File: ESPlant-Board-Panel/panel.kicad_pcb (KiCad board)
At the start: 2 copper layers, 84 x 143.7 mm, 207 parts, among them J1 Conn_01x05, U1 HC-TYPE-C-16P-01A-G, U13 ESP32-C6-MINI-1/U, U3 Reset, U4 Boot, U5 Temp/Humid-Sensor, U6 Light sensor, U7 AMS1117-3_3, U8 MK-12C02-G025

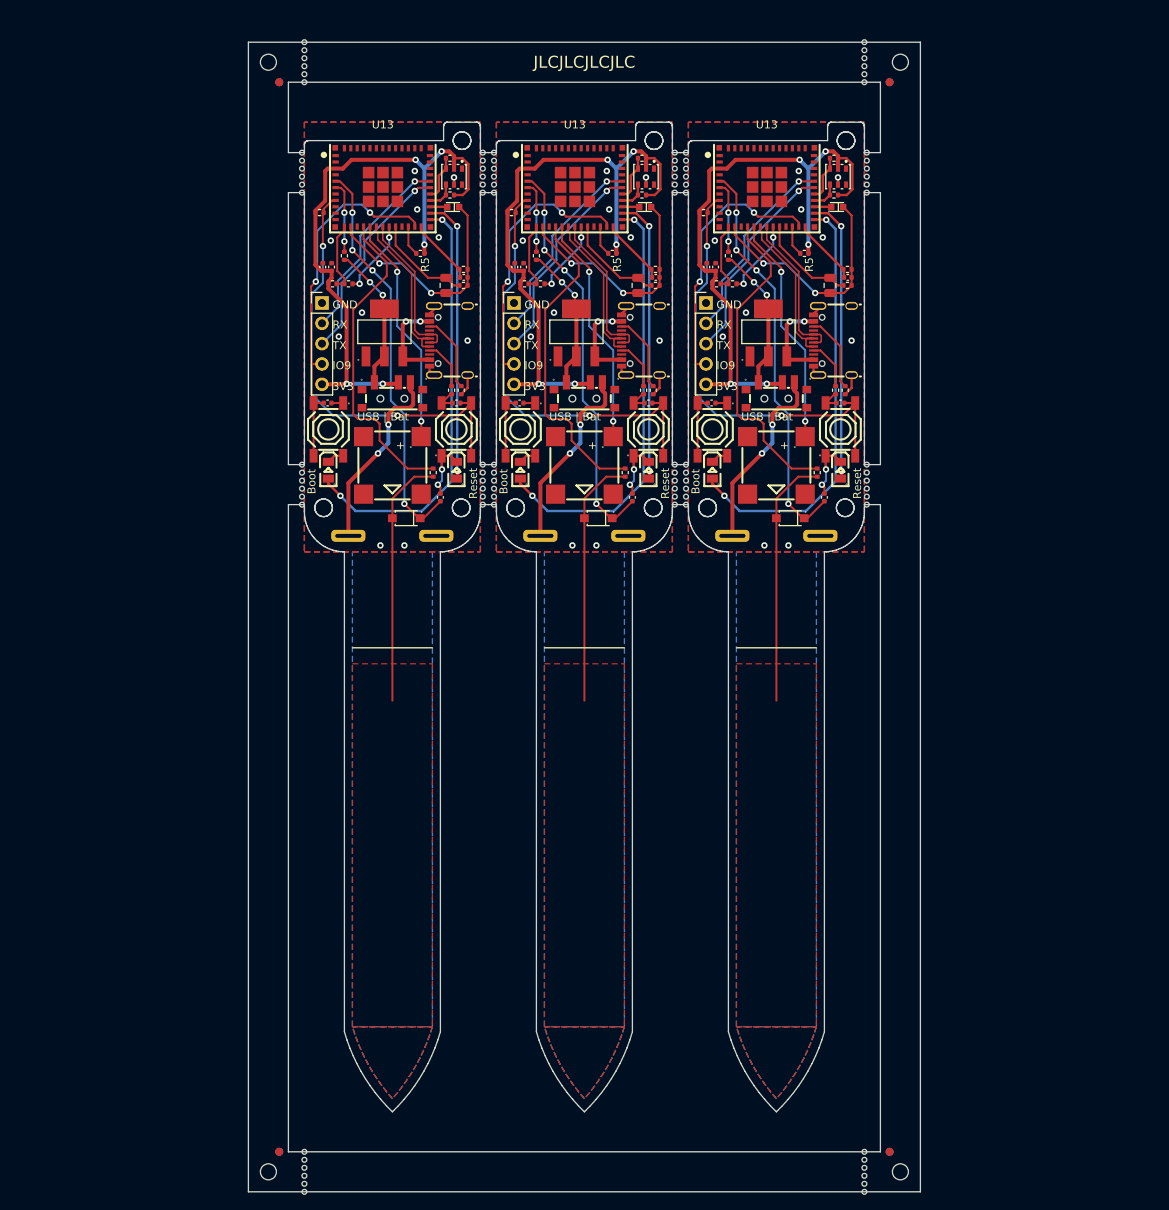
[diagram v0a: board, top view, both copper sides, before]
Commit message: Panel: Add panelization script
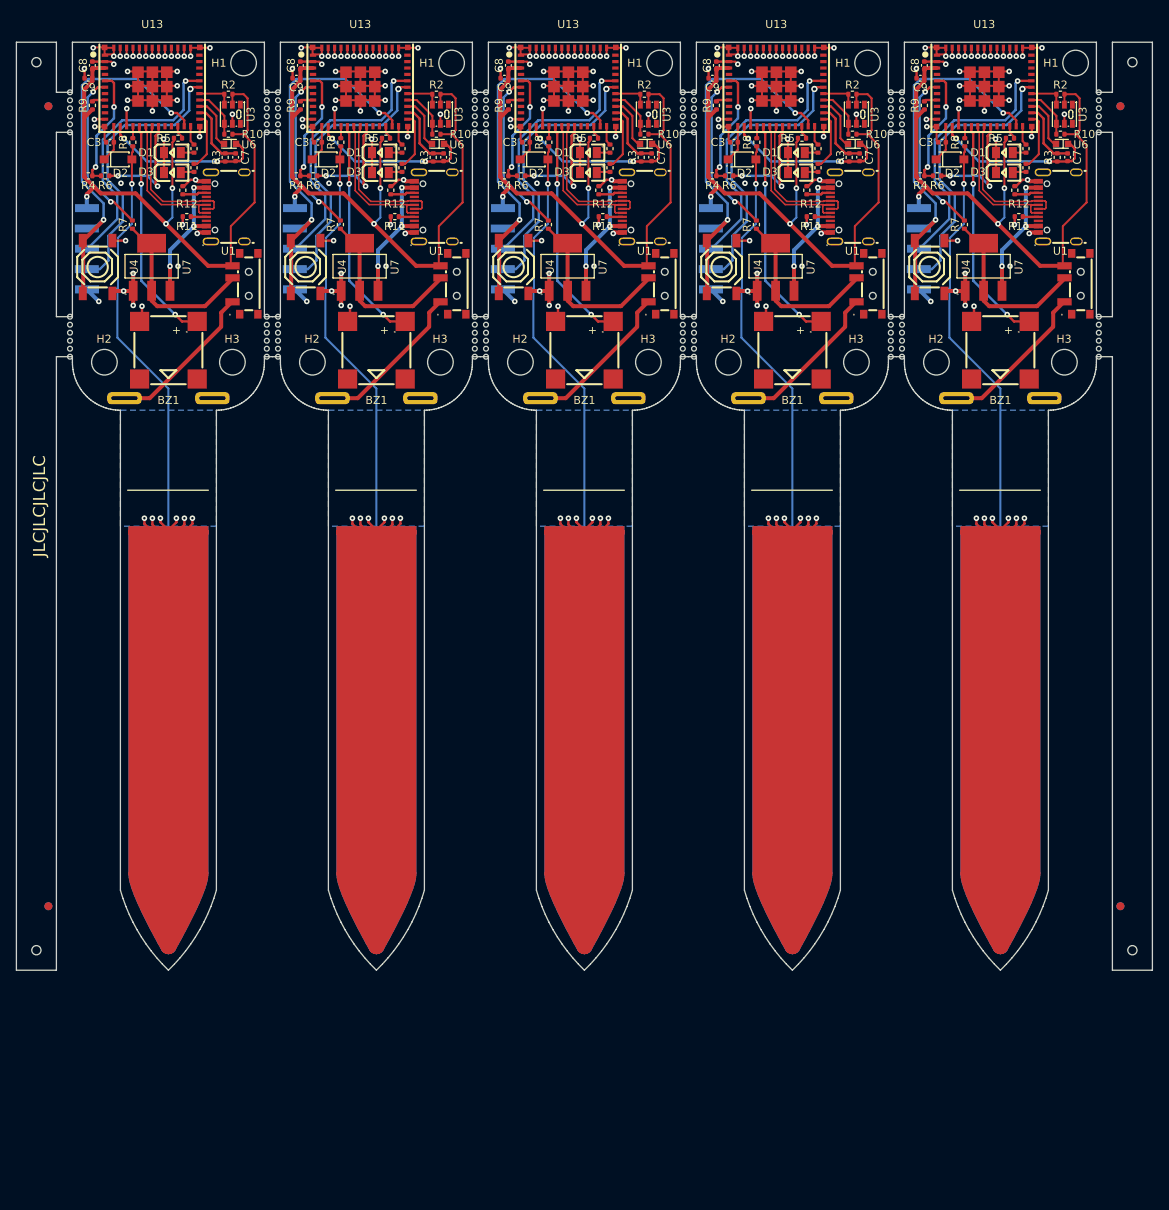
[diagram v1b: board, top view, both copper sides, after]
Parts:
- removed the BZ1 at (225.0, 72.9)
- removed the BZ1 at (201.0, 72.9)
- removed the BZ1 at (249.0, 72.9)
- removed C1 (x3), C2 (x3), C5 (x3): 100nF, Capacitor_SMD:C_0402_1005Metric
- removed the C3 at (207.0, 76.9)
- removed the C3 at (231.0, 76.9)
- removed the C3 at (255.0, 76.9)
- removed the C7 at (231.7, 50.4)
- removed the C7 at (255.7, 50.4)
- removed the C7 at (207.7, 50.4)
- removed the C8 at (193.4, 48.1)
- removed the C8 at (241.4, 48.1)
- removed the C8 at (217.4, 48.1)
- removed the C9 at (192.3, 48.1)
- removed the C9 at (240.3, 48.1)
- removed the C9 at (216.3, 48.1)
- removed the D1 at (217.0, 73.5)
- removed the D1 at (193.0, 73.5)
- removed the D1 at (241.0, 73.5)
- removed the D2 at (226.7, 79.5)
- removed the D2 at (202.7, 79.5)
- removed the D2 at (250.7, 79.5)
- removed the D3 at (209.0, 73.5)
- removed the D3 at (233.0, 73.5)
- removed the D3 at (257.0, 73.5)
- removed the J1 at (240.2, 52.6)
- removed the J1 at (216.2, 52.6)
- removed the J1 at (192.2, 52.6)
- removed R1 (x3): 10M, Resistor_SMD:R_0402_1005Metric
- removed the R10 at (256.2, 39.1)
- removed the R10 at (208.2, 39.1)
- removed the R10 at (232.2, 39.1)
- removed the R11 at (208.4, 63.5)
- removed the R11 at (232.4, 63.5)
- removed the R11 at (256.4, 63.5)
- removed the R12 at (233.6, 63.5)
- removed the R12 at (257.6, 63.5)
- removed the R12 at (209.6, 63.5)
- removed the R2 at (256.2, 34.5)
- removed the R2 at (208.2, 34.5)
- removed the R2 at (232.2, 34.5)
- removed the R3 at (233.9, 50.4)
- removed the R3 at (209.9, 50.4)
- removed the R3 at (257.9, 50.4)
- removed the R4 at (241.5, 50.2)
- removed the R4 at (217.5, 50.2)
- removed the R4 at (193.5, 50.2)
- removed the R5 at (228.5, 46.4)
- removed the R5 at (252.5, 46.4)
- removed the R5 at (204.5, 46.4)
- removed the R6 at (195.5, 50.2)
- removed the R6 at (243.5, 50.2)
- removed the R6 at (219.5, 50.2)
- removed the R7 at (219.0, 46.7)
- removed the R7 at (195.0, 46.7)
- removed the R7 at (243.0, 46.7)
- removed the R8 at (230.1, 73.8)
- removed the R8 at (254.1, 73.8)
- removed the R8 at (206.1, 73.8)
- removed the R9 at (191.9, 41.3)
- removed the R9 at (239.9, 41.3)
- removed the R9 at (215.9, 41.3)
- removed the U1 at (256.0, 57.3)
- removed the U1 at (232.0, 57.3)
- removed the U1 at (208.0, 57.3)
- removed the U13 at (247.8, 38.2)
- removed the U13 at (223.8, 38.2)
- removed the U13 at (199.8, 38.2)
- removed the U3 at (257.0, 68.4)
- removed the U3 at (209.0, 68.4)
- removed the U3 at (233.0, 68.4)
- removed the U4 at (193.0, 68.4)
- removed the U4 at (217.0, 68.4)
- removed the U4 at (241.0, 68.4)
- removed U5 (x3): Temp/Humid-Sensor, CustomFootprints:SENSOR-SMD_L3.0-W3.0-P1.00-BR
- removed the U6 at (232.6, 40.6)
- removed the U6 at (256.6, 40.6)
- removed the U6 at (208.6, 40.6)
- removed the U7 at (200.0, 56.3)
- removed the U7 at (224.0, 56.3)
- removed the U7 at (248.0, 56.3)
- removed the U8 at (201.0, 64.1)
- removed the U8 at (249.0, 64.1)
- removed the U8 at (225.0, 64.1)
- removed the U9 at (225.0, 81.7)
- removed the U9 at (249.0, 81.7)
- removed the U9 at (201.0, 81.7)
- added BZ1: Buzzer, CustomFootprints:BUZ-SMD_4P-L8.5-W8.5-P8.50-BR, F.Cu at (199.0, 58.5)
- added BZ1: Buzzer, CustomFootprints:BUZ-SMD_4P-L8.5-W8.5-P8.50-BR, F.Cu at (277.0, 58.5)
- added BZ1: Buzzer, CustomFootprints:BUZ-SMD_4P-L8.5-W8.5-P8.50-BR, F.Cu at (225.0, 58.5)
- added BZ1: Buzzer, CustomFootprints:BUZ-SMD_4P-L8.5-W8.5-P8.50-BR, F.Cu at (173.0, 58.5)
- added BZ1: Buzzer, CustomFootprints:BUZ-SMD_4P-L8.5-W8.5-P8.50-BR, F.Cu at (251.0, 58.5)
- added C3: 150pF, Capacitor_SMD:C_0402_1005Metric, F.Cu at (243.7, 32.5)
- added C3: 150pF, Capacitor_SMD:C_0402_1005Metric, F.Cu at (217.7, 32.5)
- added C3: 150pF, Capacitor_SMD:C_0402_1005Metric, F.Cu at (269.7, 32.5)
- added C3: 150pF, Capacitor_SMD:C_0402_1005Metric, F.Cu at (191.7, 32.5)
- added C3: 150pF, Capacitor_SMD:C_0402_1005Metric, F.Cu at (165.7, 32.5)
- added C4: 7pF-27pF, A=2.75cm^2, CustomFootprints:Sensor-Tip, B.Cu at (277.0, 81.0)
- added C4: 7pF-27pF, A=2.75cm^2, CustomFootprints:Sensor-Tip, B.Cu at (251.0, 81.0)
- added C4: 7pF-27pF, A=2.75cm^2, CustomFootprints:Sensor-Tip, B.Cu at (225.0, 81.0)
- added C4: 7pF-27pF, A=2.75cm^2, CustomFootprints:Sensor-Tip, B.Cu at (199.0, 81.0)
- added C4: 7pF-27pF, A=2.75cm^2, CustomFootprints:Sensor-Tip, B.Cu at (173.0, 81.0)
- added C7: 10uF, Capacitor_SMD:C_0402_1005Metric, F.Cu at (181.4, 34.4)
- added C7: 10uF, Capacitor_SMD:C_0402_1005Metric, F.Cu at (259.4, 34.4)
- added C7: 10uF, Capacitor_SMD:C_0402_1005Metric, F.Cu at (233.4, 34.4)
- added C7: 10uF, Capacitor_SMD:C_0402_1005Metric, F.Cu at (285.4, 34.4)
- added C7: 10uF, Capacitor_SMD:C_0402_1005Metric, F.Cu at (207.4, 34.4)
- added C8: 10nF, Capacitor_SMD:C_0402_1005Metric, F.Cu at (215.5, 22.9)
- added C8: 10nF, Capacitor_SMD:C_0402_1005Metric, F.Cu at (267.5, 22.9)
- added C8: 10nF, Capacitor_SMD:C_0402_1005Metric, F.Cu at (163.5, 22.9)
- added C8: 10nF, Capacitor_SMD:C_0402_1005Metric, F.Cu at (241.5, 22.9)
- added C8: 10nF, Capacitor_SMD:C_0402_1005Metric, F.Cu at (189.5, 22.9)
- added C9: 10uF, Capacitor_SMD:C_0402_1005Metric, F.Cu at (241.0, 24.5)
- added C9: 10uF, Capacitor_SMD:C_0402_1005Metric, F.Cu at (163.0, 24.5)
- added C9: 10uF, Capacitor_SMD:C_0402_1005Metric, F.Cu at (215.0, 24.5)
- added C9: 10uF, Capacitor_SMD:C_0402_1005Metric, F.Cu at (267.0, 24.5)
- added C9: 10uF, Capacitor_SMD:C_0402_1005Metric, F.Cu at (189.0, 24.5)
- added D1: GREEN, CustomFootprints:LED0805-R-RD, F.Cu at (199.5, 33.8)
- added D1: GREEN, CustomFootprints:LED0805-R-RD, F.Cu at (225.5, 33.8)
- added D1: GREEN, CustomFootprints:LED0805-R-RD, F.Cu at (251.5, 33.8)
- added D1: GREEN, CustomFootprints:LED0805-R-RD, F.Cu at (277.5, 33.8)
- added D1: GREEN, CustomFootprints:LED0805-R-RD, F.Cu at (173.5, 33.8)
- added D2: SOD-123-Switching-Diode, CustomFootprints:SOD-123F_L2.7-W1.6-LS3.8-RD, F.Cu at (166.7, 34.6)
- added D2: SOD-123-Switching-Diode, CustomFootprints:SOD-123F_L2.7-W1.6-LS3.8-RD, F.Cu at (270.7, 34.6)
- added D2: SOD-123-Switching-Diode, CustomFootprints:SOD-123F_L2.7-W1.6-LS3.8-RD, F.Cu at (218.7, 34.6)
- added D2: SOD-123-Switching-Diode, CustomFootprints:SOD-123F_L2.7-W1.6-LS3.8-RD, F.Cu at (192.7, 34.6)
- added D2: SOD-123-Switching-Diode, CustomFootprints:SOD-123F_L2.7-W1.6-LS3.8-RD, F.Cu at (244.7, 34.6)
- added D3: RED, CustomFootprints:LED0805-R-RD, F.Cu at (251.5, 36.3)
- added D3: RED, CustomFootprints:LED0805-R-RD, F.Cu at (173.5, 36.3)
- added D3: RED, CustomFootprints:LED0805-R-RD, F.Cu at (225.5, 36.3)
- added D3: RED, CustomFootprints:LED0805-R-RD, F.Cu at (199.5, 36.3)
- added D3: RED, CustomFootprints:LED0805-R-RD, F.Cu at (277.5, 36.3)
- added H1: MountingHole, MountingHole:MountingHole_3.2mm_M3, F.Cu at (182.4, 22.6)
- added H1: MountingHole, MountingHole:MountingHole_3.2mm_M3, F.Cu at (286.4, 22.6)
- added H1: MountingHole, MountingHole:MountingHole_3.2mm_M3, F.Cu at (234.4, 22.6)
- added H1: MountingHole, MountingHole:MountingHole_3.2mm_M3, F.Cu at (208.4, 22.6)
- added H1: MountingHole, MountingHole:MountingHole_3.2mm_M3, F.Cu at (260.4, 22.6)
- added H2: MountingHole, MountingHole:MountingHole_3.2mm_M3, F.Cu at (243.0, 60.0)
- added H2: MountingHole, MountingHole:MountingHole_3.2mm_M3, F.Cu at (217.0, 60.0)
- added H2: MountingHole, MountingHole:MountingHole_3.2mm_M3, F.Cu at (269.0, 60.0)
- added H2: MountingHole, MountingHole:MountingHole_3.2mm_M3, F.Cu at (191.0, 60.0)
- added H2: MountingHole, MountingHole:MountingHole_3.2mm_M3, F.Cu at (165.0, 60.0)
- added H3: MountingHole, MountingHole:MountingHole_3.2mm_M3, F.Cu at (181.0, 60.0)
- added H3: MountingHole, MountingHole:MountingHole_3.2mm_M3, F.Cu at (233.0, 60.0)
- added H3: MountingHole, MountingHole:MountingHole_3.2mm_M3, F.Cu at (285.0, 60.0)
- added H3: MountingHole, MountingHole:MountingHole_3.2mm_M3, F.Cu at (207.0, 60.0)
- added H3: MountingHole, MountingHole:MountingHole_3.2mm_M3, F.Cu at (259.0, 60.0)
- added J1: Conn_01x05, CustomFootprints:PinHeader_1x05_P2.54mm_Vertical_SMD, B.Cu at (216.1, 45.8)
- added J1: Conn_01x05, CustomFootprints:PinHeader_1x05_P2.54mm_Vertical_SMD, B.Cu at (164.1, 45.8)
- added J1: Conn_01x05, CustomFootprints:PinHeader_1x05_P2.54mm_Vertical_SMD, B.Cu at (268.1, 45.8)
- added J1: Conn_01x05, CustomFootprints:PinHeader_1x05_P2.54mm_Vertical_SMD, B.Cu at (242.1, 45.8)
- added J1: Conn_01x05, CustomFootprints:PinHeader_1x05_P2.54mm_Vertical_SMD, B.Cu at (190.1, 45.8)
- added KiKit_MB_17_1: NPTH, NPTH, F.Cu at (289.3, 31.3)
- added KiKit_MB_17_2: NPTH, NPTH, F.Cu at (289.3, 30.3)
- added KiKit_MB_17_3: NPTH, NPTH, F.Cu at (289.3, 29.3)
- added KiKit_MB_17_4: NPTH, NPTH, F.Cu at (289.3, 28.3)
- added KiKit_MB_17_5: NPTH, NPTH, F.Cu at (289.3, 27.3)
- added KiKit_MB_17_6: NPTH, NPTH, F.Cu at (289.3, 26.3)
- added KiKit_MB_18_1: NPTH, NPTH, F.Cu at (264.7, 26.3)
- added KiKit_MB_18_2: NPTH, NPTH, F.Cu at (264.7, 27.3)
- added KiKit_MB_18_3: NPTH, NPTH, F.Cu at (264.7, 28.3)
- added KiKit_MB_18_4: NPTH, NPTH, F.Cu at (264.7, 29.3)
- added KiKit_MB_18_5: NPTH, NPTH, F.Cu at (264.7, 30.3)
- added KiKit_MB_18_6: NPTH, NPTH, F.Cu at (264.7, 31.3)
- added KiKit_MB_19_1: NPTH, NPTH, F.Cu at (264.7, 54.3)
- added KiKit_MB_19_2: NPTH, NPTH, F.Cu at (264.7, 55.3)
- added KiKit_MB_19_3: NPTH, NPTH, F.Cu at (264.7, 56.3)
- added KiKit_MB_19_4: NPTH, NPTH, F.Cu at (264.7, 57.3)
- added KiKit_MB_19_5: NPTH, NPTH, F.Cu at (264.7, 58.3)
- added KiKit_MB_19_6: NPTH, NPTH, F.Cu at (264.7, 59.3)
- added KiKit_MB_20_1: NPTH, NPTH, F.Cu at (289.3, 59.3)
- added KiKit_MB_20_2: NPTH, NPTH, F.Cu at (289.3, 58.3)
- added KiKit_MB_20_3: NPTH, NPTH, F.Cu at (289.3, 57.3)
- added KiKit_MB_20_4: NPTH, NPTH, F.Cu at (289.3, 56.3)
- added KiKit_MB_20_5: NPTH, NPTH, F.Cu at (289.3, 55.3)
- added KiKit_MB_20_6: NPTH, NPTH, F.Cu at (289.3, 54.3)
- added R10: 5k1, Resistor_SMD:R_0402_1005Metric, F.Cu at (284.5, 31.5)
- added R10: 5k1, Resistor_SMD:R_0402_1005Metric, F.Cu at (258.5, 31.5)
- added R10: 5k1, Resistor_SMD:R_0402_1005Metric, F.Cu at (206.5, 31.5)
- added R10: 5k1, Resistor_SMD:R_0402_1005Metric, F.Cu at (232.5, 31.5)
- added R10: 5k1, Resistor_SMD:R_0402_1005Metric, F.Cu at (180.5, 31.5)
- added R11: 5k1, Resistor_SMD:R_0402_1005Metric, F.Cu at (279.3, 41.8)
- added R11: 5k1, Resistor_SMD:R_0402_1005Metric, F.Cu at (253.3, 41.8)
- added R11: 5k1, Resistor_SMD:R_0402_1005Metric, F.Cu at (175.3, 41.8)
- added R11: 5k1, Resistor_SMD:R_0402_1005Metric, F.Cu at (201.3, 41.8)
- added R11: 5k1, Resistor_SMD:R_0402_1005Metric, F.Cu at (227.3, 41.8)
- added R12: 5k1, Resistor_SMD:R_0402_1005Metric, F.Cu at (252.8, 38.5)
- added R12: 5k1, Resistor_SMD:R_0402_1005Metric, F.Cu at (174.8, 38.5)
- added R12: 5k1, Resistor_SMD:R_0402_1005Metric, F.Cu at (278.8, 38.5)
- added R12: 5k1, Resistor_SMD:R_0402_1005Metric, F.Cu at (226.8, 38.5)
- added R12: 5k1, Resistor_SMD:R_0402_1005Metric, F.Cu at (200.8, 38.5)
- added R13: 120, Resistor_SMD:R_0402_1005Metric, F.Cu at (176.2, 33.3)
- added R13: 120, Resistor_SMD:R_0402_1005Metric, F.Cu at (228.2, 33.3)
- added R13: 120, Resistor_SMD:R_0402_1005Metric, F.Cu at (202.2, 33.3)
- added R13: 120, Resistor_SMD:R_0402_1005Metric, F.Cu at (254.2, 33.3)
- added R13: 120, Resistor_SMD:R_0402_1005Metric, F.Cu at (280.2, 33.3)
- added R14: 120, Resistor_SMD:R_0402_1005Metric, F.Cu at (176.2, 35.7)
- added R14: 120, Resistor_SMD:R_0402_1005Metric, F.Cu at (254.2, 35.7)
- added R14: 120, Resistor_SMD:R_0402_1005Metric, F.Cu at (280.2, 35.7)
- added R14: 120, Resistor_SMD:R_0402_1005Metric, F.Cu at (228.2, 35.7)
- added R14: 120, Resistor_SMD:R_0402_1005Metric, F.Cu at (202.2, 35.7)
- added R2: 5k1, Resistor_SMD:R_0402_1005Metric, F.Cu at (232.5, 26.5)
- added R2: 5k1, Resistor_SMD:R_0402_1005Metric, F.Cu at (180.5, 26.5)
- added R2: 5k1, Resistor_SMD:R_0402_1005Metric, F.Cu at (258.5, 26.5)
- added R2: 5k1, Resistor_SMD:R_0402_1005Metric, F.Cu at (206.5, 26.5)
- added R2: 5k1, Resistor_SMD:R_0402_1005Metric, F.Cu at (284.5, 26.5)
- added R3: 47k, Resistor_SMD:R_0402_1005Metric, F.Cu at (232.1, 34.4)
- added R3: 47k, Resistor_SMD:R_0402_1005Metric, F.Cu at (206.1, 34.4)
- added R3: 47k, Resistor_SMD:R_0402_1005Metric, F.Cu at (284.1, 34.4)
- added R3: 47k, Resistor_SMD:R_0402_1005Metric, F.Cu at (180.1, 34.4)
- added R3: 47k, Resistor_SMD:R_0402_1005Metric, F.Cu at (258.1, 34.4)
- added R4: 5k1, Resistor_SMD:R_0402_1005Metric, F.Cu at (215.0, 36.7)
- added R4: 5k1, Resistor_SMD:R_0402_1005Metric, F.Cu at (241.0, 36.7)
- added R4: 5k1, Resistor_SMD:R_0402_1005Metric, F.Cu at (163.0, 36.7)
- added R4: 5k1, Resistor_SMD:R_0402_1005Metric, F.Cu at (267.0, 36.7)
- added R4: 5k1, Resistor_SMD:R_0402_1005Metric, F.Cu at (189.0, 36.7)
- added R5: 10k, Resistor_SMD:R_0402_1005Metric, F.Cu at (174.2, 32.0)
- added R5: 10k, Resistor_SMD:R_0402_1005Metric, F.Cu at (278.2, 32.0)
- added R5: 10k, Resistor_SMD:R_0402_1005Metric, F.Cu at (200.2, 32.0)
- added R5: 10k, Resistor_SMD:R_0402_1005Metric, F.Cu at (252.2, 32.0)
- added R5: 10k, Resistor_SMD:R_0402_1005Metric, F.Cu at (226.2, 32.0)
- added R6: 2k, Resistor_SMD:R_0402_1005Metric, F.Cu at (191.1, 36.7)
- added R6: 2k, Resistor_SMD:R_0402_1005Metric, F.Cu at (165.1, 36.7)
- added R6: 2k, Resistor_SMD:R_0402_1005Metric, F.Cu at (217.1, 36.7)
- added R6: 2k, Resistor_SMD:R_0402_1005Metric, F.Cu at (269.1, 36.7)
- added R6: 2k, Resistor_SMD:R_0402_1005Metric, F.Cu at (243.1, 36.7)
- added R7: 10k, Resistor_SMD:R_0402_1005Metric, F.Cu at (194.5, 42.8)
- added R7: 10k, Resistor_SMD:R_0402_1005Metric, F.Cu at (168.5, 42.8)
- added R7: 10k, Resistor_SMD:R_0402_1005Metric, F.Cu at (246.5, 42.8)
- added R7: 10k, Resistor_SMD:R_0402_1005Metric, F.Cu at (220.5, 42.8)
- added R7: 10k, Resistor_SMD:R_0402_1005Metric, F.Cu at (272.5, 42.8)
- added R8: 10k, Resistor_SMD:R_0402_1005Metric, F.Cu at (272.6, 32.5)
- added R8: 10k, Resistor_SMD:R_0402_1005Metric, F.Cu at (168.6, 32.5)
- added R8: 10k, Resistor_SMD:R_0402_1005Metric, F.Cu at (194.6, 32.5)
- added R8: 10k, Resistor_SMD:R_0402_1005Metric, F.Cu at (220.6, 32.5)
- added R8: 10k, Resistor_SMD:R_0402_1005Metric, F.Cu at (246.6, 32.5)
- added R9: 10k, Resistor_SMD:R_0402_1005Metric, F.Cu at (215.5, 27.9)
- added R9: 10k, Resistor_SMD:R_0402_1005Metric, F.Cu at (189.5, 27.9)
- added R9: 10k, Resistor_SMD:R_0402_1005Metric, F.Cu at (241.5, 27.9)
- added R9: 10k, Resistor_SMD:R_0402_1005Metric, F.Cu at (267.5, 27.9)
- added R9: 10k, Resistor_SMD:R_0402_1005Metric, F.Cu at (163.5, 27.9)
- added U1: HC-TYPE-C-16P-01A-G, CustomFootprints:USB-C-SMD_G-SWITCH_GT-USB-7010EN, F.Cu at (206.1, 40.6)
- added U1: HC-TYPE-C-16P-01A-G, CustomFootprints:USB-C-SMD_G-SWITCH_GT-USB-7010EN, F.Cu at (258.1, 40.6)
- added U1: HC-TYPE-C-16P-01A-G, CustomFootprints:USB-C-SMD_G-SWITCH_GT-USB-7010EN, F.Cu at (284.1, 40.6)
- added U1: HC-TYPE-C-16P-01A-G, CustomFootprints:USB-C-SMD_G-SWITCH_GT-USB-7010EN, F.Cu at (232.1, 40.6)
- added U1: HC-TYPE-C-16P-01A-G, CustomFootprints:USB-C-SMD_G-SWITCH_GT-USB-7010EN, F.Cu at (180.1, 40.6)
- added U13: ESP32-C6-MINI-1/U, CustomFootprints:WIFIM-SMD_61P-L16.6-W13.2-P0.80-ESP32-C6-MINI-1-N4, F.Cu at (275.0, 25.6)
- added U13: ESP32-C6-MINI-1/U, CustomFootprints:WIFIM-SMD_61P-L16.6-W13.2-P0.80-ESP32-C6-MINI-1-N4, F.Cu at (197.0, 25.6)
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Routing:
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- added copper zone on In1.Cu, net Board_0-GND
- added copper zone on In2.Cu, net Board_0-GND
- added copper zone on In1.Cu, net Board_1-GND
- added copper zone on In2.Cu, net Board_1-GND
- added copper zone on In1.Cu, net Board_2-GND
- added copper zone on In2.Cu, net Board_2-GND
- added copper zone on B.Cu, net Board_3-GND
- added copper zone on In1.Cu, net Board_3-GND
- added copper zone on In2.Cu, net Board_3-GND
- added copper zone on B.Cu, net Board_4-GND
- added copper zone on In1.Cu, net Board_4-GND
- added copper zone on In2.Cu, net Board_4-GND
- removed copper zone on F.Cu, net Board_0-/SensorCapV
- removed copper zone on F.Cu, net Board_0-GND
- removed copper zone on F.Cu, net Board_1-/SensorCapV
- removed copper zone on F.Cu, net Board_1-GND
- removed copper zone on F.Cu, net Board_2-/SensorCapV
- removed copper zone on F.Cu, net Board_2-GND
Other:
- board size 84 x 143.7 mm -> 142 x 116 mm
- copper layers 2 -> 4
- board text added: "Aconitum"
- board text added: "Blumy"
- board text removed: "3V3"
- board text removed: "Boot"
- board text removed: "ESPlant-v2.1"
- board text removed: "GND"
- board text removed: "IO9"
- board text removed: "M2"
- board text removed: "RX"
- board text removed: "Reset"
- board text removed: "TX"
- board text removed: "USB | Bat"

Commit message: Board: New power supply chip
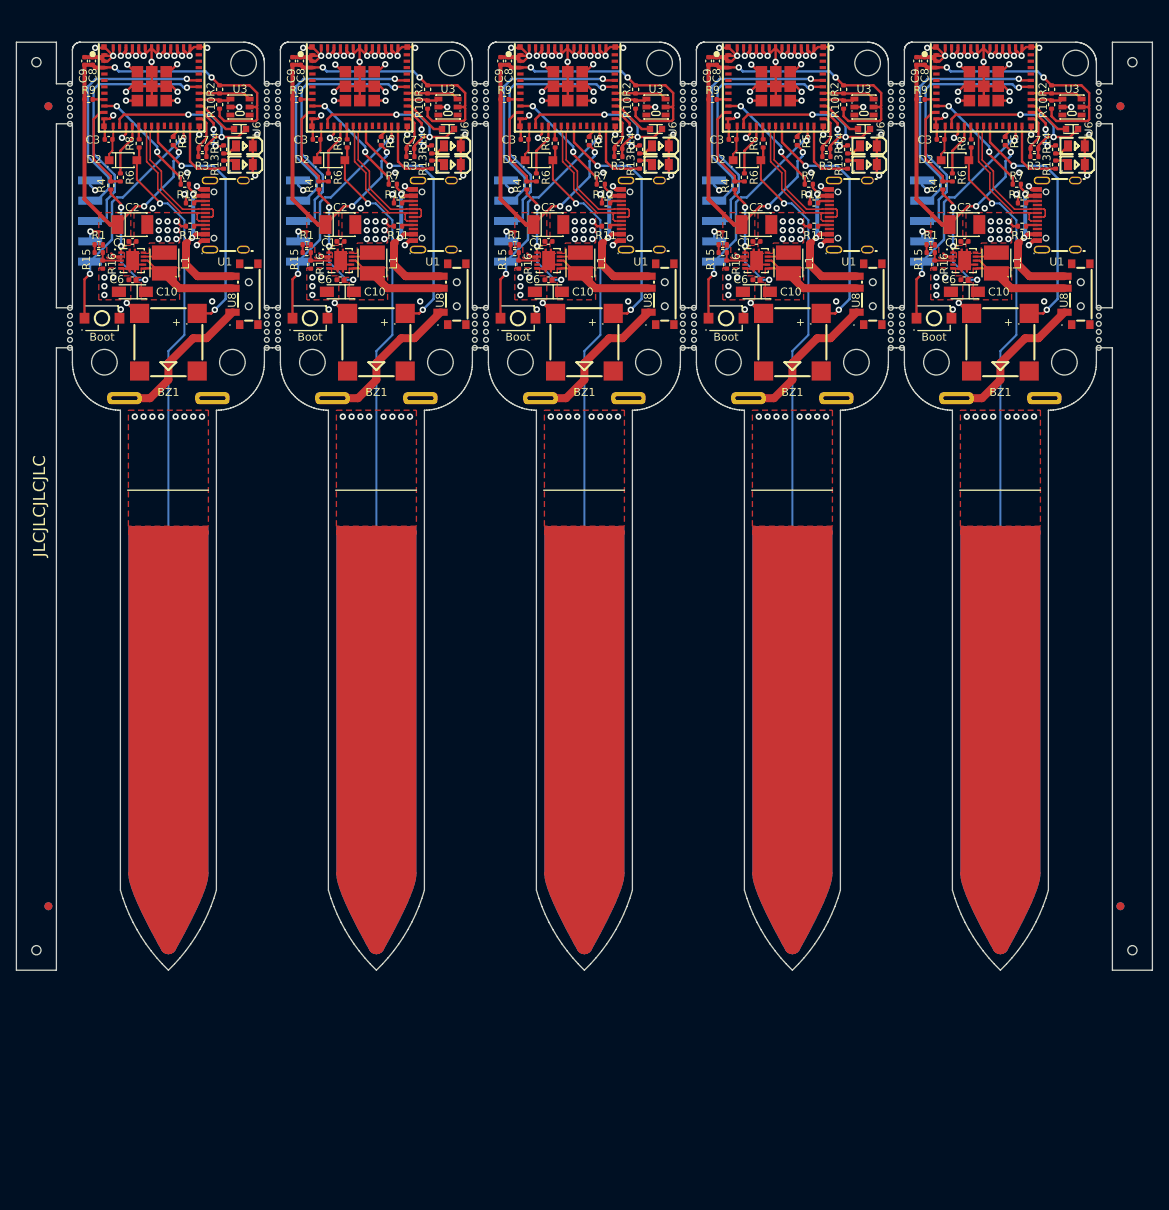
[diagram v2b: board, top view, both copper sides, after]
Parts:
- removed the BZ1 at (199.0, 58.5)
- removed the BZ1 at (277.0, 58.5)
- removed the BZ1 at (225.0, 58.5)
- removed the BZ1 at (173.0, 58.5)
- removed the BZ1 at (251.0, 58.5)
- removed the C3 at (243.7, 32.5)
- removed the C3 at (217.7, 32.5)
- removed the C3 at (269.7, 32.5)
- removed the C3 at (191.7, 32.5)
- removed the C3 at (165.7, 32.5)
- removed the C7 at (181.4, 34.4)
- removed the C7 at (259.4, 34.4)
- removed the C7 at (233.4, 34.4)
- removed the C7 at (285.4, 34.4)
- removed the C7 at (207.4, 34.4)
- removed the C8 at (215.5, 22.9)
- removed the C8 at (267.5, 22.9)
- removed the C8 at (163.5, 22.9)
- removed the C8 at (241.5, 22.9)
- removed the C8 at (189.5, 22.9)
- removed the C9 at (241.0, 24.5)
- removed the C9 at (163.0, 24.5)
- removed the C9 at (215.0, 24.5)
- removed the C9 at (267.0, 24.5)
- removed the C9 at (189.0, 24.5)
- removed the D1 at (199.5, 33.8)
- removed the D1 at (225.5, 33.8)
- removed the D1 at (251.5, 33.8)
- removed the D1 at (277.5, 33.8)
- removed the D1 at (173.5, 33.8)
- removed the D2 at (166.7, 34.6)
- removed the D2 at (270.7, 34.6)
- removed the D2 at (218.7, 34.6)
- removed the D2 at (192.7, 34.6)
- removed the D2 at (244.7, 34.6)
- removed the D3 at (251.5, 36.3)
- removed the D3 at (173.5, 36.3)
- removed the D3 at (225.5, 36.3)
- removed the D3 at (199.5, 36.3)
- removed the D3 at (277.5, 36.3)
- removed the J1 at (216.1, 45.8)
- removed the J1 at (164.1, 45.8)
- removed the J1 at (268.1, 45.8)
- removed the J1 at (242.1, 45.8)
- removed the J1 at (190.1, 45.8)
- removed the R10 at (284.5, 31.5)
- removed the R10 at (258.5, 31.5)
- removed the R10 at (206.5, 31.5)
- removed the R10 at (232.5, 31.5)
- removed the R10 at (180.5, 31.5)
- removed the R11 at (279.3, 41.8)
- removed the R11 at (253.3, 41.8)
- removed the R11 at (175.3, 41.8)
- removed the R11 at (201.3, 41.8)
- removed the R11 at (227.3, 41.8)
- removed the R12 at (252.8, 38.5)
- removed the R12 at (174.8, 38.5)
- removed the R12 at (278.8, 38.5)
- removed the R12 at (226.8, 38.5)
- removed the R12 at (200.8, 38.5)
- removed the R13 at (176.2, 33.3)
- removed the R13 at (228.2, 33.3)
- removed the R13 at (202.2, 33.3)
- removed the R13 at (254.2, 33.3)
- removed the R13 at (280.2, 33.3)
- removed the R14 at (176.2, 35.7)
- removed the R14 at (254.2, 35.7)
- removed the R14 at (280.2, 35.7)
- removed the R14 at (228.2, 35.7)
- removed the R14 at (202.2, 35.7)
- removed the R2 at (232.5, 26.5)
- removed the R2 at (180.5, 26.5)
- removed the R2 at (258.5, 26.5)
- removed the R2 at (206.5, 26.5)
- removed the R2 at (284.5, 26.5)
- removed the R3 at (232.1, 34.4)
- removed the R3 at (206.1, 34.4)
- removed the R3 at (284.1, 34.4)
- removed the R3 at (180.1, 34.4)
- removed the R3 at (258.1, 34.4)
- removed the R4 at (215.0, 36.7)
- removed the R4 at (241.0, 36.7)
- removed the R4 at (163.0, 36.7)
- removed the R4 at (267.0, 36.7)
- removed the R4 at (189.0, 36.7)
- removed the R5 at (174.2, 32.0)
- removed the R5 at (278.2, 32.0)
- removed the R5 at (200.2, 32.0)
- removed the R5 at (252.2, 32.0)
- removed the R5 at (226.2, 32.0)
- removed the R6 at (191.1, 36.7)
- removed the R6 at (165.1, 36.7)
- removed the R6 at (217.1, 36.7)
- removed the R6 at (269.1, 36.7)
- removed the R6 at (243.1, 36.7)
- removed the R7 at (194.5, 42.8)
- removed the R7 at (168.5, 42.8)
- removed the R7 at (246.5, 42.8)
- removed the R7 at (220.5, 42.8)
- removed the R7 at (272.5, 42.8)
- removed the R8 at (272.6, 32.5)
- removed the R8 at (168.6, 32.5)
- removed the R8 at (194.6, 32.5)
- removed the R8 at (220.6, 32.5)
- removed the R8 at (246.6, 32.5)
- removed the R9 at (215.5, 27.9)
- removed the R9 at (189.5, 27.9)
- removed the R9 at (241.5, 27.9)
- removed the R9 at (267.5, 27.9)
- removed the R9 at (163.5, 27.9)
- removed the U1 at (206.1, 40.6)
- removed the U1 at (258.1, 40.6)
- removed the U1 at (284.1, 40.6)
- removed the U1 at (232.1, 40.6)
- removed the U1 at (180.1, 40.6)
- removed the U13 at (275.0, 25.6)
- removed the U13 at (197.0, 25.6)
- removed the U13 at (223.0, 25.6)
- removed the U13 at (171.0, 25.6)
- removed the U13 at (249.0, 25.6)
- removed the U3 at (285.0, 29.0)
- removed the U3 at (233.0, 29.0)
- removed the U3 at (207.0, 29.0)
- removed the U3 at (181.0, 29.0)
- removed the U3 at (259.0, 29.0)
- removed U4 (x5): Button, CustomFootprints:SW-SMD_4P-L5.1-W5.1-P3.70-LS6.5-TL-2
- removed the U6 at (284.7, 32.7)
- removed the U6 at (206.7, 32.7)
- removed the U6 at (258.7, 32.7)
- removed the U6 at (180.7, 32.7)
- removed the U6 at (232.7, 32.7)
- removed the U7 at (170.9, 48.1)
- removed the U7 at (274.9, 48.1)
- removed the U7 at (222.9, 48.1)
- removed the U7 at (196.9, 48.1)
- removed the U7 at (248.9, 48.1)
- removed the U8 at (208.6, 50.2)
- removed the U8 at (286.6, 50.2)
- removed the U8 at (260.6, 50.2)
- removed the U8 at (234.6, 50.2)
- removed the U8 at (182.6, 50.2)
- added BZ1: Buzzer, CustomFootprints:BUZ-SMD_4P-L8.5-W8.5-P8.50-BR, F.Cu at (277.0, 57.5)
- added BZ1: Buzzer, CustomFootprints:BUZ-SMD_4P-L8.5-W8.5-P8.50-BR, F.Cu at (251.0, 57.5)
- added BZ1: Buzzer, CustomFootprints:BUZ-SMD_4P-L8.5-W8.5-P8.50-BR, F.Cu at (225.0, 57.5)
- added BZ1: Buzzer, CustomFootprints:BUZ-SMD_4P-L8.5-W8.5-P8.50-BR, F.Cu at (199.0, 57.5)
- added BZ1: Buzzer, CustomFootprints:BUZ-SMD_4P-L8.5-W8.5-P8.50-BR, F.Cu at (173.0, 57.5)
- added C1: 2.2uF-Ceramic, Capacitor_SMD:C_0402_1005Metric, F.Cu at (168.5, 44.9)
- added C1: 2.2uF-Ceramic, Capacitor_SMD:C_0402_1005Metric, F.Cu at (220.5, 44.9)
- added C1: 2.2uF-Ceramic, Capacitor_SMD:C_0402_1005Metric, F.Cu at (272.5, 44.9)
- added C1: 2.2uF-Ceramic, Capacitor_SMD:C_0402_1005Metric, F.Cu at (194.5, 44.9)
- added C1: 2.2uF-Ceramic, Capacitor_SMD:C_0402_1005Metric, F.Cu at (246.5, 44.9)
- added C10: 10uF-Tantalum, CustomFootprints:CAP-SMD_L3.2-W1.6-RD-C7171, F.Cu at (220.5, 51.2)
- added C10: 10uF-Tantalum, CustomFootprints:CAP-SMD_L3.2-W1.6-RD-C7171, F.Cu at (272.5, 51.2)
- added C10: 10uF-Tantalum, CustomFootprints:CAP-SMD_L3.2-W1.6-RD-C7171, F.Cu at (194.5, 51.2)
- added C10: 10uF-Tantalum, CustomFootprints:CAP-SMD_L3.2-W1.6-RD-C7171, F.Cu at (246.5, 51.2)
- added C10: 10uF-Tantalum, CustomFootprints:CAP-SMD_L3.2-W1.6-RD-C7171, F.Cu at (168.5, 51.2)
- added C2: 100uF-Tantalum, CustomFootprints:CASE-B_3528, F.Cu at (168.5, 42.8)
- added C2: 100uF-Tantalum, CustomFootprints:CASE-B_3528, F.Cu at (194.5, 42.8)
- added C2: 100uF-Tantalum, CustomFootprints:CASE-B_3528, F.Cu at (272.5, 42.8)
- added C2: 100uF-Tantalum, CustomFootprints:CASE-B_3528, F.Cu at (246.5, 42.8)
- added C2: 100uF-Tantalum, CustomFootprints:CASE-B_3528, F.Cu at (220.5, 42.8)
- added C3: 10nF, Capacitor_SMD:C_0402_1005Metric, F.Cu at (217.5, 32.2)
- added C3: 10nF, Capacitor_SMD:C_0402_1005Metric, F.Cu at (165.5, 32.2)
- added C3: 10nF, Capacitor_SMD:C_0402_1005Metric, F.Cu at (243.5, 32.2)
- added C3: 10nF, Capacitor_SMD:C_0402_1005Metric, F.Cu at (191.5, 32.2)
- added C3: 10nF, Capacitor_SMD:C_0402_1005Metric, F.Cu at (269.5, 32.2)
- added C6: 100nF-Ceramic, Capacitor_SMD:C_0402_1005Metric, F.Cu at (220.5, 49.7)
- added C6: 100nF-Ceramic, Capacitor_SMD:C_0402_1005Metric, F.Cu at (246.5, 49.7)
- added C6: 100nF-Ceramic, Capacitor_SMD:C_0402_1005Metric, F.Cu at (168.5, 49.7)
- added C6: 100nF-Ceramic, Capacitor_SMD:C_0402_1005Metric, F.Cu at (194.5, 49.7)
- added C6: 100nF-Ceramic, Capacitor_SMD:C_0402_1005Metric, F.Cu at (272.5, 49.7)
- added C7: 10uF, Capacitor_SMD:C_0402_1005Metric, F.Cu at (229.3, 33.3)
- added C7: 10uF, Capacitor_SMD:C_0402_1005Metric, F.Cu at (203.3, 33.3)
- added C7: 10uF, Capacitor_SMD:C_0402_1005Metric, F.Cu at (281.3, 33.3)
- added C7: 10uF, Capacitor_SMD:C_0402_1005Metric, F.Cu at (177.3, 33.3)
- added C7: 10uF, Capacitor_SMD:C_0402_1005Metric, F.Cu at (255.3, 33.3)
- added C8: 10nF, Capacitor_SMD:C_0402_1005Metric, F.Cu at (267.5, 22.4)
- added C8: 10nF, Capacitor_SMD:C_0402_1005Metric, F.Cu at (215.5, 22.4)
- added C8: 10nF, Capacitor_SMD:C_0402_1005Metric, F.Cu at (241.5, 22.4)
- added C8: 10nF, Capacitor_SMD:C_0402_1005Metric, F.Cu at (163.5, 22.4)
- added C8: 10nF, Capacitor_SMD:C_0402_1005Metric, F.Cu at (189.5, 22.4)
- added C9: 10uF, Capacitor_SMD:C_0402_1005Metric, F.Cu at (162.5, 22.4)
- added C9: 10uF, Capacitor_SMD:C_0402_1005Metric, F.Cu at (214.5, 22.4)
- added C9: 10uF, Capacitor_SMD:C_0402_1005Metric, F.Cu at (266.5, 22.4)
- added C9: 10uF, Capacitor_SMD:C_0402_1005Metric, F.Cu at (188.5, 22.4)
- added C9: 10uF, Capacitor_SMD:C_0402_1005Metric, F.Cu at (240.5, 22.4)
- added D1: GREEN, CustomFootprints:LED0805-R-RD, F.Cu at (234.5, 35.3)
- added D1: GREEN, CustomFootprints:LED0805-R-RD, F.Cu at (182.5, 35.3)
- added D1: GREEN, CustomFootprints:LED0805-R-RD, F.Cu at (208.5, 35.3)
- added D1: GREEN, CustomFootprints:LED0805-R-RD, F.Cu at (286.5, 35.3)
- added D1: GREEN, CustomFootprints:LED0805-R-RD, F.Cu at (260.5, 35.3)
- added D2: SOD-123-Switching-Diode, CustomFootprints:SOD-123F_L2.7-W1.6-LS3.8-RD, F.Cu at (193.3, 34.8)
- added D2: SOD-123-Switching-Diode, CustomFootprints:SOD-123F_L2.7-W1.6-LS3.8-RD, F.Cu at (167.3, 34.8)
- added D2: SOD-123-Switching-Diode, CustomFootprints:SOD-123F_L2.7-W1.6-LS3.8-RD, F.Cu at (271.3, 34.8)
- added D2: SOD-123-Switching-Diode, CustomFootprints:SOD-123F_L2.7-W1.6-LS3.8-RD, F.Cu at (219.3, 34.8)
- added D2: SOD-123-Switching-Diode, CustomFootprints:SOD-123F_L2.7-W1.6-LS3.8-RD, F.Cu at (245.3, 34.8)
- added D3: RED, CustomFootprints:LED0805-R-RD, F.Cu at (208.5, 33.0)
- added D3: RED, CustomFootprints:LED0805-R-RD, F.Cu at (260.5, 33.0)
- added D3: RED, CustomFootprints:LED0805-R-RD, F.Cu at (182.5, 33.0)
- added D3: RED, CustomFootprints:LED0805-R-RD, F.Cu at (234.5, 33.0)
- added D3: RED, CustomFootprints:LED0805-R-RD, F.Cu at (286.5, 33.0)
- added J1: Conn_01x05, CustomFootprints:PinHeader_1x05_P2.54mm_Vertical_SMD, B.Cu at (265.9, 42.4)
- added J1: Conn_01x05, CustomFootprints:PinHeader_1x05_P2.54mm_Vertical_SMD, B.Cu at (213.9, 42.4)
- added J1: Conn_01x05, CustomFootprints:PinHeader_1x05_P2.54mm_Vertical_SMD, B.Cu at (161.9, 42.4)
- added J1: Conn_01x05, CustomFootprints:PinHeader_1x05_P2.54mm_Vertical_SMD, B.Cu at (239.9, 42.4)
- added J1: Conn_01x05, CustomFootprints:PinHeader_1x05_P2.54mm_Vertical_SMD, B.Cu at (187.9, 42.4)
- added L1: CD32YP0302-6R8M, CustomFootprints:IND-SMD_L3.5-W3.0, F.Cu at (172.5, 47.6)
- added L1: CD32YP0302-6R8M, CustomFootprints:IND-SMD_L3.5-W3.0, F.Cu at (224.5, 47.6)
- added L1: CD32YP0302-6R8M, CustomFootprints:IND-SMD_L3.5-W3.0, F.Cu at (276.5, 47.6)
- added L1: CD32YP0302-6R8M, CustomFootprints:IND-SMD_L3.5-W3.0, F.Cu at (250.5, 47.6)
- added L1: CD32YP0302-6R8M, CustomFootprints:IND-SMD_L3.5-W3.0, F.Cu at (198.5, 47.6)
- added R1: 100k, Resistor_SMD:R_0402_1005Metric, F.Cu at (268.3, 45.3)
- added R1: 100k, Resistor_SMD:R_0402_1005Metric, F.Cu at (190.3, 45.3)
- added R1: 100k, Resistor_SMD:R_0402_1005Metric, F.Cu at (216.3, 45.3)
- added R1: 100k, Resistor_SMD:R_0402_1005Metric, F.Cu at (242.3, 45.3)
- added R1: 100k, Resistor_SMD:R_0402_1005Metric, F.Cu at (164.3, 45.3)
- added R10: 5k1, Resistor_SMD:R_0402_1005Metric, F.Cu at (205.4, 27.8)
- added R10: 5k1, Resistor_SMD:R_0402_1005Metric, F.Cu at (179.4, 27.8)
- added R10: 5k1, Resistor_SMD:R_0402_1005Metric, F.Cu at (257.4, 27.8)
- added R10: 5k1, Resistor_SMD:R_0402_1005Metric, F.Cu at (283.4, 27.8)
- added R10: 5k1, Resistor_SMD:R_0402_1005Metric, F.Cu at (231.4, 27.8)
- added R11: 5k1, Resistor_SMD:R_0402_1005Metric, F.Cu at (201.7, 43.0)
- added R11: 5k1, Resistor_SMD:R_0402_1005Metric, F.Cu at (279.7, 43.0)
- added R11: 5k1, Resistor_SMD:R_0402_1005Metric, F.Cu at (253.7, 43.0)
- added R11: 5k1, Resistor_SMD:R_0402_1005Metric, F.Cu at (175.7, 43.0)
- added R11: 5k1, Resistor_SMD:R_0402_1005Metric, F.Cu at (227.7, 43.0)
- added R12: 5k1, Resistor_SMD:R_0402_1005Metric, F.Cu at (279.7, 40.1)
- added R12: 5k1, Resistor_SMD:R_0402_1005Metric, F.Cu at (227.7, 40.1)
- added R12: 5k1, Resistor_SMD:R_0402_1005Metric, F.Cu at (253.7, 40.1)
- added R12: 5k1, Resistor_SMD:R_0402_1005Metric, F.Cu at (201.7, 40.1)
- added R12: 5k1, Resistor_SMD:R_0402_1005Metric, F.Cu at (175.7, 40.1)
- added R13: 120, Resistor_SMD:R_0402_1005Metric, F.Cu at (283.9, 35.3)
- added R13: 120, Resistor_SMD:R_0402_1005Metric, F.Cu at (179.9, 35.3)
- added R13: 120, Resistor_SMD:R_0402_1005Metric, F.Cu at (205.9, 35.3)
- added R13: 120, Resistor_SMD:R_0402_1005Metric, F.Cu at (231.9, 35.3)
- added R13: 120, Resistor_SMD:R_0402_1005Metric, F.Cu at (257.9, 35.3)
- added R14: 120, Resistor_SMD:R_0402_1005Metric, F.Cu at (205.9, 33.4)
- added R14: 120, Resistor_SMD:R_0402_1005Metric, F.Cu at (179.9, 33.4)
- added R14: 120, Resistor_SMD:R_0402_1005Metric, F.Cu at (257.9, 33.4)
- added R14: 120, Resistor_SMD:R_0402_1005Metric, F.Cu at (283.9, 33.4)
- added R14: 120, Resistor_SMD:R_0402_1005Metric, F.Cu at (231.9, 33.4)
- added R15: 1M, Resistor_SMD:R_0402_1005Metric, F.Cu at (268.3, 46.3)
- added R15: 1M, Resistor_SMD:R_0402_1005Metric, F.Cu at (242.3, 46.3)
- added R15: 1M, Resistor_SMD:R_0402_1005Metric, F.Cu at (164.3, 46.3)
- added R15: 1M, Resistor_SMD:R_0402_1005Metric, F.Cu at (216.3, 46.3)
- added R15: 1M, Resistor_SMD:R_0402_1005Metric, F.Cu at (190.3, 46.3)
- added R16: 200k, Resistor_SMD:R_0402_1005Metric, F.Cu at (190.8, 47.8)
- added R16: 200k, Resistor_SMD:R_0402_1005Metric, F.Cu at (268.8, 47.8)
- added R16: 200k, Resistor_SMD:R_0402_1005Metric, F.Cu at (164.8, 47.8)
- added R16: 200k, Resistor_SMD:R_0402_1005Metric, F.Cu at (216.8, 47.8)
- added R16: 200k, Resistor_SMD:R_0402_1005Metric, F.Cu at (242.8, 47.8)
- added R2: 5k1, Resistor_SMD:R_0402_1005Metric, F.Cu at (179.4, 25.9)
- added R2: 5k1, Resistor_SMD:R_0402_1005Metric, F.Cu at (231.4, 25.9)
- added R2: 5k1, Resistor_SMD:R_0402_1005Metric, F.Cu at (205.4, 25.9)
- added R2: 5k1, Resistor_SMD:R_0402_1005Metric, F.Cu at (283.4, 25.9)
- added R2: 5k1, Resistor_SMD:R_0402_1005Metric, F.Cu at (257.4, 25.9)
- added R3: 47k, Resistor_SMD:R_0402_1005Metric, F.Cu at (177.3, 34.3)
- added R3: 47k, Resistor_SMD:R_0402_1005Metric, F.Cu at (203.3, 34.3)
- added R3: 47k, Resistor_SMD:R_0402_1005Metric, F.Cu at (229.3, 34.3)
- added R3: 47k, Resistor_SMD:R_0402_1005Metric, F.Cu at (281.3, 34.3)
- added R3: 47k, Resistor_SMD:R_0402_1005Metric, F.Cu at (255.3, 34.3)
- added R4: 5k1, Resistor_SMD:R_0402_1005Metric, F.Cu at (191.8, 37.9)
- added R4: 5k1, Resistor_SMD:R_0402_1005Metric, F.Cu at (269.8, 37.9)
- added R4: 5k1, Resistor_SMD:R_0402_1005Metric, F.Cu at (217.8, 37.9)
- added R4: 5k1, Resistor_SMD:R_0402_1005Metric, F.Cu at (165.8, 37.9)
- added R4: 5k1, Resistor_SMD:R_0402_1005Metric, F.Cu at (243.8, 37.9)
- added R5: 10k, Resistor_SMD:R_0402_1005Metric, F.Cu at (225.6, 32.4)
- added R5: 10k, Resistor_SMD:R_0402_1005Metric, F.Cu at (277.6, 32.4)
- added R5: 10k, Resistor_SMD:R_0402_1005Metric, F.Cu at (199.6, 32.4)
- added R5: 10k, Resistor_SMD:R_0402_1005Metric, F.Cu at (173.6, 32.4)
- added R5: 10k, Resistor_SMD:R_0402_1005Metric, F.Cu at (251.6, 32.4)
- added R6: 2k, Resistor_SMD:R_0402_1005Metric, F.Cu at (219.0, 36.9)
- added R6: 2k, Resistor_SMD:R_0402_1005Metric, F.Cu at (271.0, 36.9)
- added R6: 2k, Resistor_SMD:R_0402_1005Metric, F.Cu at (245.0, 36.9)
- added R6: 2k, Resistor_SMD:R_0402_1005Metric, F.Cu at (167.0, 36.9)
- added R6: 2k, Resistor_SMD:R_0402_1005Metric, F.Cu at (193.0, 36.9)
- added R7: 10k, Resistor_SMD:R_0402_1005Metric, F.Cu at (175.1, 37.8)
- added R7: 10k, Resistor_SMD:R_0402_1005Metric, F.Cu at (201.1, 37.8)
- added R7: 10k, Resistor_SMD:R_0402_1005Metric, F.Cu at (253.1, 37.8)
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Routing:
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- added copper zone on F.Cu, net Board_0-+3V3
- added copper zone on F.Cu, net Board_0-GND
- added copper zone on F.Cu, net Board_0-VCC
- added copper zone on F.Cu, net Board_1-+3V3
- added copper zone on F.Cu, net Board_1-GND
- added copper zone on F.Cu, net Board_1-VCC
- added copper zone on F.Cu, net Board_2-+3V3
- added copper zone on F.Cu, net Board_2-GND
- added copper zone on F.Cu, net Board_2-VCC
- added copper zone on F.Cu, net Board_3-+3V3
- added copper zone on F.Cu, net Board_3-GND
- added copper zone on F.Cu, net Board_3-VCC
- added copper zone on F.Cu, net Board_4-+3V3
- added copper zone on F.Cu, net Board_4-GND
- added copper zone on F.Cu, net Board_4-VCC
- removed copper zone on B.Cu, net Board_0-GND
- removed copper zone on B.Cu, net Board_1-GND
- removed copper zone on B.Cu, net Board_2-GND
- removed copper zone on B.Cu, net Board_3-GND
- removed copper zone on B.Cu, net Board_4-GND
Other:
- outline, holes or cut-outs redrawn
- board text added: "Boot"
